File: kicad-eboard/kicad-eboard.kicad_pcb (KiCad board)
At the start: 2 copper layers, 89 parts, among them J1 Conn_02x03, J2 Conn_01x02, J3 Conn_01x10, M1 Hopper_Servo, SW1 LIMIT_1, SW2 LIMIT_2, SW3 SRX_Encoder, U1 TinkerBoard, U10 REF2033, U11 PDQ15-Q24-S12-D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

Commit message: Work from IPRO
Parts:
- C6, C7, R9, U6: moved to B.Cu
- moved TP2 66.1 mm to (133.5, 8.00)
- moved R4 65.5 mm to (140.0, 19.5)
- moved C5 58.1 mm to (132.8, 22.0), turned to 90 degrees
- moved R3 57.6 mm to (147.0, 19.5)
- moved U6 51.5 mm to (132.5, 22.0), turned to 90 degrees
- moved TP15 45.1 mm to (80.4, -9.20)
- moved TP9 45.1 mm to (80.4, -12.4)
- moved TP12 45.1 mm to (80.7, -2.40)
- moved TP11 45.1 mm to (78.0, 1.15)
- moved TP14 45.1 mm to (80.4, -5.95)
- moved TP13 43.6 mm to (80.0, -19.1)
- moved TP4 40.1 mm to (151.5, 26.8)
- moved R2 40.0 mm to (140.0, 28.0)
- moved TP10 38.0 mm to (114.0, 69.5)
- moved R9 33.7 mm to (137.2, 22.0), turned to 0 degrees
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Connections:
- C5 pad 1: +3V3 -> +3.3VADC
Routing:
- net /M3-: track 0.00 -> 24.1 mm
- net Net-(C7-Pad1): track 26.6 -> 2.70 mm, vias 0 -> 1
- net Net-(C7-Pad2): track 24.6 -> 2.53 mm, vias 0 -> 1
- net GNDREF: track 25.2 -> 4.04 mm
- net /M1-: track 0.00 -> 20.3 mm
- net Net-(C7-Pad3): track 22.4 -> 2.44 mm, vias 0 -> 1
- net /M3+: track 0.00 -> 17.6 mm
- net Net-(C7-Pad4): track 19.4 -> 2.54 mm, vias 0 -> 1
- net /M6+: track 16.4 -> 0.00 mm
- net /M5-: track 15.9 -> 0.00 mm
- net /M1+: track 0.00 -> 15.3 mm
- net /M5+: track 14.3 -> 0.00 mm
- net +1.65V: track 19.7 -> 6.09 mm, vias 3 -> 1
- net /M8-: track 16.6 -> 29.7 mm
- net /M2-: track 0.00 -> 11.3 mm
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- added copper zone on F.Cu, net +1.65V
- added copper zone on B.Cu, net GNDREF

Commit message: Add PTC fuse
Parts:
- added F1: 6A, 2019Spacehawks:Fuse_Littelfuse_16R600G, F.Cu at (82.0, 25.0)
- added H1: MountingHole, MountingHole:MountingHole_2.7mm_M2.5_Pad, F.Cu at (232.5, 69.0)
- added H2: MountingHole, MountingHole:MountingHole_2.7mm_M2.5_Pad, F.Cu at (232.5, 147.0)
- added H3: MountingHole, MountingHole:MountingHole_2.7mm_M2.5_Pad, F.Cu at (281.5, 69.0)
- added H4: MountingHole, MountingHole:MountingHole_2.7mm_M2.5_Pad, F.Cu at (281.5, 147.0)
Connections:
- J2 pad 1: +BATT -> Net-(F1-Pad1)
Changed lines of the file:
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@@
-(kicad_pcb (version 20171130) (host pcbnew "(5.1.5)-3")
+(kicad_pcb (version 20171130) (host pcbnew 5.0.2+dfsg1-1)
   (general
     (thickness 1.6)
@@
     (tracks 316)
     (zones 0)
-    (modules 89)
-    (nets 97)
+    (modules 94)
+    (nets 98)
   )
   (page A4)
@@
     (zone_45_only no)
     (trace_min 0.1778)
+    (segment_width 0.2)
+    (edge_width 0.15)
     (via_size 0.8)
     (via_drill 0.4)
@@
     (uvia_min_size 0.2)
     (uvia_min_drill 0.1)
-    (edge_width 0.15)
-    (segment_width 0.2)
     (pcb_text_width 0.3)
     (pcb_text_size 1.5 1.5)
@@
   (net 95 "Net-(C12-Pad1)")
   (net 96 "Net-(C11-Pad1)")
+  (net 97 "Net-(F1-Pad1)")
   (net_class Default "This is the default net class."
     (clearance 0.2)
@@
     (add_net "Net-(C7-Pad3)")
     (add_net "Net-(C7-Pad4)")
+    (add_net "Net-(F1-Pad1)")
     (add_net "Net-(M1-Pad1)")
     (add_net "Net-(M1-Pad4)")
@@
     (uvia_drill 0.1)
   )
+  (module 2019Spacehawks:Fuse_Littelfuse_16R600G (layer F.Cu)
+    (at 82 25)
+    (tags "PTC resettable fuse")
+    (fp_text reference F1 (at 0 0.5) (layer F.SilkS)
+      (effects (font (size 1 1) (thickness 0.15)))
+    )
+    (fp_text value 6A (at 0 -0.5) (layer F.Fab)
+      (effects (font (size 1 1) (thickness 0.15)))
+    )
+    (fp_line (start -5.2 -1.5) (end 5.2 -1.5) (layer F.SilkS) (width 0.15))
+    (fp_line (start 5.2 -1.5) (end 5.2 1.5) (layer F.SilkS) (width 0.15))
+    (fp_line (start -5.2 1.5) (end 5.2 1.5) (layer F.SilkS) (width 0.15))
+    (fp_line (start -5.2 -1.5) (end -5.2 1.5) (layer F.SilkS) (width 0.15))
+    (fp_line (start -5.4 -1.7) (end 5.4 -1.7) (layer F.CrtYd) (width 0.15))
+    (fp_line (start -5.4 -1.7) (end -5.4 1.7) (layer F.CrtYd) (width 0.15))
+    (fp_line (start -5.4 1.7) (end 5.4 1.7) (layer F.CrtYd) (width 0.15))
+    (fp_line (start 5.4 -1.7) (end 5.4 1.7) (layer F.CrtYd) (width 0.15))
+    (pad 1 thru_hole circle (at -2.55 -0.6) (size 1.524 1.524) (drill 0.83) (layers *.Cu *.Mask)
+      (net 97 "Net-(F1-Pad1)"))
+    (pad 2 thru_hole circle (at 2.55 0.6) (size 1.524 1.524) (drill 0.83) (layers *.Cu *.Mask)
+      (net 3 +BATT))
+  )
+  (module MountingHole:MountingHole_2.7mm_M2.5_Pad (layer F.Cu)
+    (at 281.5 147)
+    (descr "Mounting Hole 2.7mm, M2.5")
+    (tags "mounting hole 2.7mm m2.5")
+    (attr virtual)
+    (fp_text reference H4 (at 0 -3.7) (layer F.SilkS)
+      (effects (font (size 1 1) (thickness 0.15)))
+    )
+    (fp_text value MountingHole (at 0 3.7) (layer F.Fab)
+      (effects (font (size 1 1) (thickness 0.15)))
+    )
+    (fp_circle (center 0 0) (end 2.95 0) (layer F.CrtYd) (width 0.05))
+    (fp_circle (center 0 0) (end 2.7 0) (layer Cmts.User) (width 0.15))
+    (fp_text user %R (at 0.3 0) (layer F.Fab)
+      (effects (font (size 1 1) (thickness 0.15)))
+    )
+    (pad 1 thru_hole circle (at 0 0) (size 5.4 5.4) (drill 2.7) (layers *.Cu *.Mask))
+  )
+  (module MountingHole:MountingHole_2.7mm_M2.5_Pad (layer F.Cu)
+    (at 281.5 69)
+    (descr "Mounting Hole 2.7mm, M2.5")
+    (tags "mounting hole 2.7mm m2.5")
+    (attr virtual)
+    (fp_text reference H3 (at 0 -3.7) (layer F.SilkS)
+      (effects (font (size 1 1) (thickness 0.15)))
+    )
+    (fp_text value MountingHole (at 0 3.7) (layer F.Fab)
+      (effects (font (size 1 1) (thickness 0.15)))
+    )
+    (fp_text user %R (at 0.3 0) (layer F.Fab)
+      (effects (font (size 1 1) (thickness 0.15)))
+    )
+    (fp_circle (center 0 0) (end 2.7 0) (layer Cmts.User) (width 0.15))
+    (fp_circle (center 0 0) (end 2.95 0) (layer F.CrtYd) (width 0.05))
+    (pad 1 thru_hole circle (at 0 0) (size 5.4 5.4) (drill 2.7) (layers *.Cu *.Mask))
+  )
+  (module MountingHole:MountingHole_2.7mm_M2.5_Pad (layer F.Cu)
+    (at 232.5 147)
+    (descr "Mounting Hole 2.7mm, M2.5")
+    (tags "mounting hole 2.7mm m2.5")
+    (attr virtual)
+    (fp_text reference H2 (at 0 -3.7) (layer F.SilkS)
+      (effects (font (size 1 1) (thickness 0.15)))
+    )
+    (fp_text value MountingHole (at 0 3.7) (layer F.Fab)
+      (effects (font (size 1 1) (thickness 0.15)))
+    )
+    (fp_circle (center 0 0) (end 2.95 0) (layer F.CrtYd) (width 0.05))
+    (fp_circle (center 0 0) (end 2.7 0) (layer Cmts.User) (width 0.15))
+    (fp_text user %R (at 0.3 0) (layer F.Fab)
+      (effects (font (size 1 1) (thickness 0.15)))
+    )
+    (pad 1 thru_hole circle (at 0 0) (size 5.4 5.4) (drill 2.7) (layers *.Cu *.Mask))
+  )
+  (module MountingHole:MountingHole_2.7mm_M2.5_Pad (layer F.Cu)
+    (at 232.5 69)
+    (descr "Mounting Hole 2.7mm, M2.5")
+    (tags "mounting hole 2.7mm m2.5")
+    (attr virtual)
+    (fp_text reference H1 (at 0 -3.7) (layer F.SilkS)
+      (effects (font (size 1 1) (thickness 0.15)))
+    )
+    (fp_text value MountingHole (at 0 3.7) (layer F.Fab)
+      (effects (font (size 1 1) (thickness 0.15)))
+    )
+    (fp_text user %R (at 0.3 0) (layer F.Fab)
+      (effects (font (size 1 1) (thickness 0.15)))
+    )
+    (fp_circle (center 0 0) (end 2.7 0) (layer Cmts.User) (width 0.15))
+    (fp_circle (center 0 0) (end 2.95 0) (layer F.CrtYd) (width 0.05))
+    (pad 1 thru_hole circle (at 0 0) (size 5.4 5.4) (drill 2.7) (layers *.Cu *.Mask))
+  )
   (module Package_SO:TSSOP-20_4.4x6.5mm_P0.65mm (layer F.Cu)
     (at 132.5 30 90)
@@
       (net 2 GNDPWR))
     (pad 1 thru_hole rect (at -3.95 0 270) (size 6.25 2.25) (drill oval 5.23 1.27) (layers *.Cu *.Mask)
-      (net 3 +BATT))
+      (net 97 "Net-(F1-Pad1)"))
     (model ${KIPRJMOD}/2019Spacehawks.pretty/Powerpole_45A_Vert_01x02.wrl
       (at (xyz 0 0 0))
@@
   (gr_arc (start 281.5 69) (end 285 69) (angle -90) (layer F.SilkS) (width 0.2))
   (gr_arc (start 232.5 69) (end 232.5 65.5) (angle -90) (layer F.SilkS) (width 0.2))
-  (gr_line (start 285 150.5) (end 232.5 150.5) (layer F.SilkS) (width 0.2))
-  (gr_line (start 285 69) (end 285 150.5) (layer F.SilkS) (width 0.2))
+  (gr_line (start 281.5 150.5) (end 232.5 150.5) (layer F.SilkS) (width 0.2))
+  (gr_line (start 285 69) (end 285 147) (layer F.SilkS) (width 0.2))
   (gr_line (start 232.5 65.5) (end 281.5 65.5) (layer F.SilkS) (width 0.2))
   (gr_line (start 229 147) (end 229 69) (layer F.SilkS) (width 0.2))

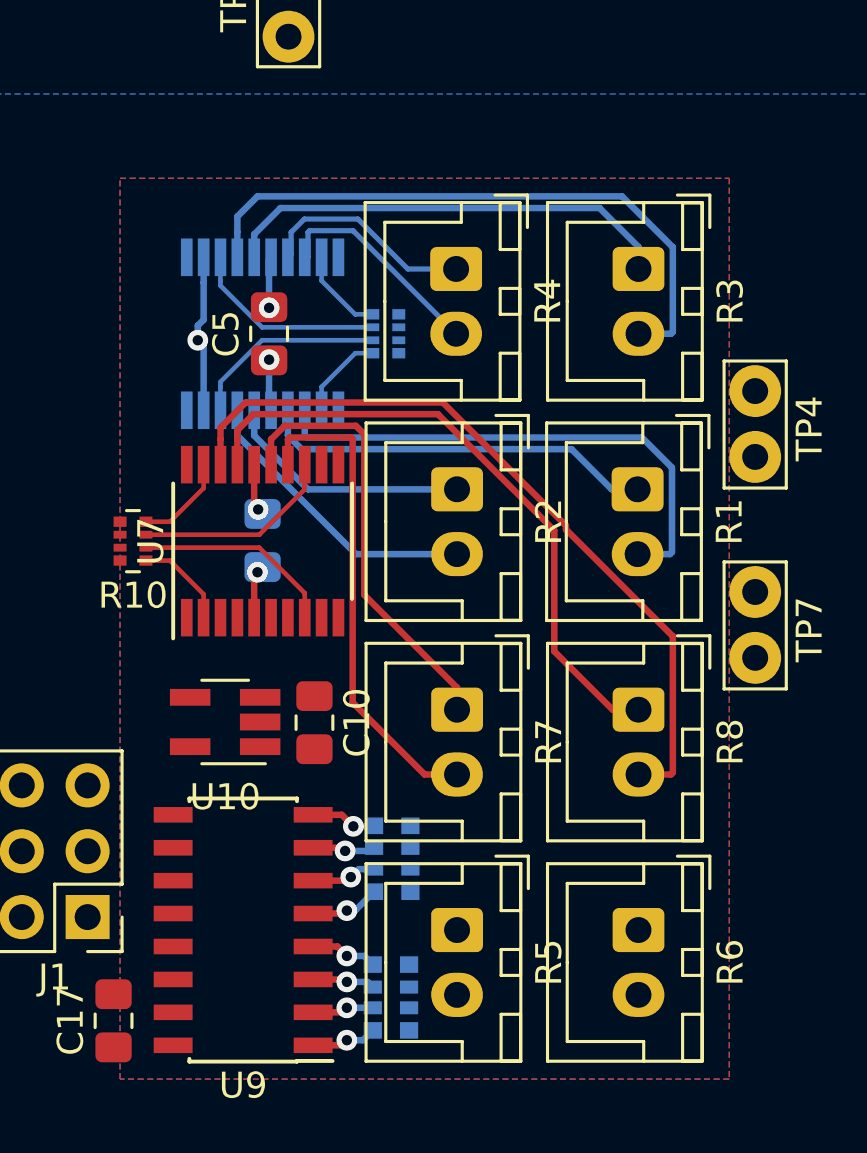
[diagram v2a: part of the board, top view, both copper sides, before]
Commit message: Route differential pairs
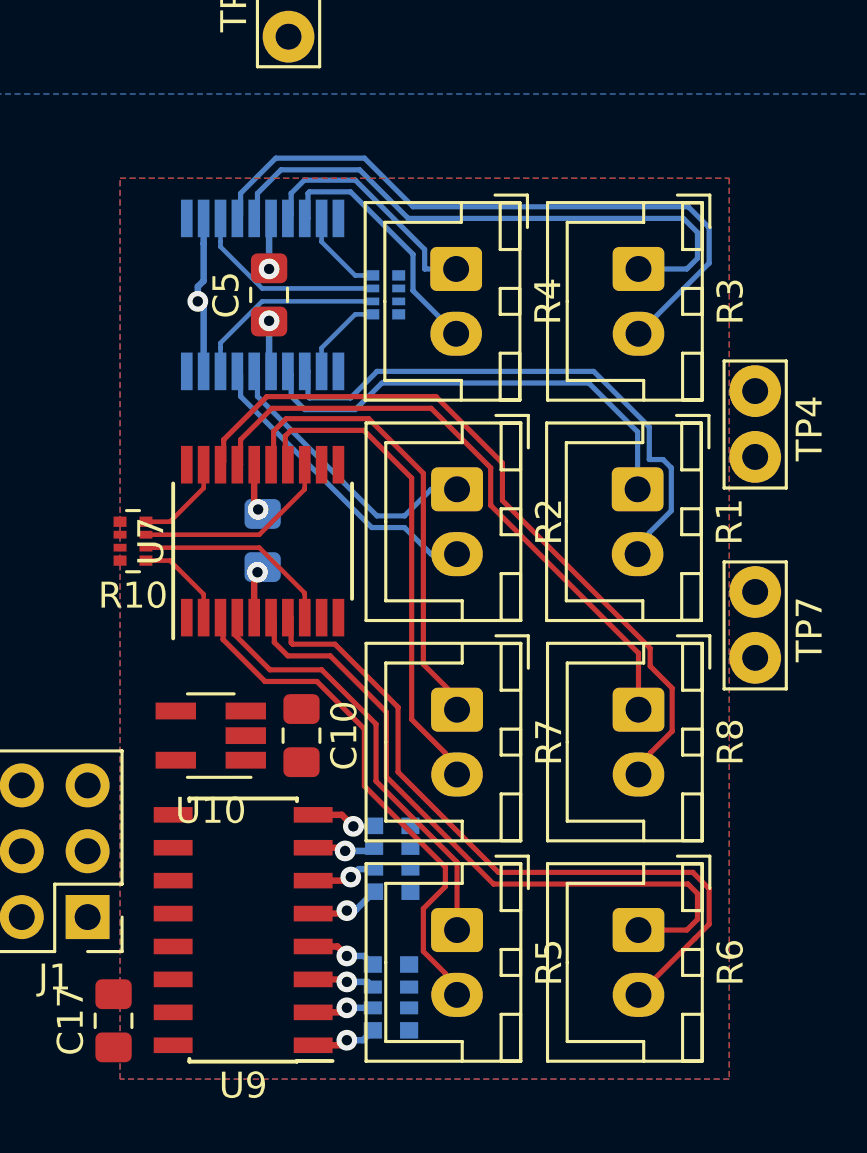
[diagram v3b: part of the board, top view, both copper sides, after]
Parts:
- moved C5 1.50 mm to (132.8, 20.5)
- moved R9 1.50 mm to (137.2, 20.5)
- moved U6 1.50 mm to (132.5, 20.5)
- moved U10 0.76 mm to (130.5, 37.5)
- moved C10 0.71 mm to (134.0, 37.5)
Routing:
- net /M6-: track 0.00 -> 27.8 mm
- net /M6+: track 0.00 -> 26.2 mm
- net /M5-: track 0.00 -> 20.2 mm
- net /M5+: track 0.00 -> 16.8 mm
- net /M3+: track 17.6 -> 22.9 mm
- net /M1+: track 15.3 -> 18.0 mm
- net /M3-: track 24.1 -> 26.0 mm
- net /M4-: track 8.48 -> 9.92 mm
- net /M1-: track 20.3 -> 21.7 mm
- net /M2+: track 9.66 -> 11.1 mm
- net /M4+: track 8.39 -> 9.45 mm
- net /M8-: track 29.7 -> 28.8 mm
- net /M7+: track 17.0 -> 17.8 mm
- net /M8+: track 24.5 -> 23.9 mm
- net /M2-: track 11.3 -> 11.9 mm

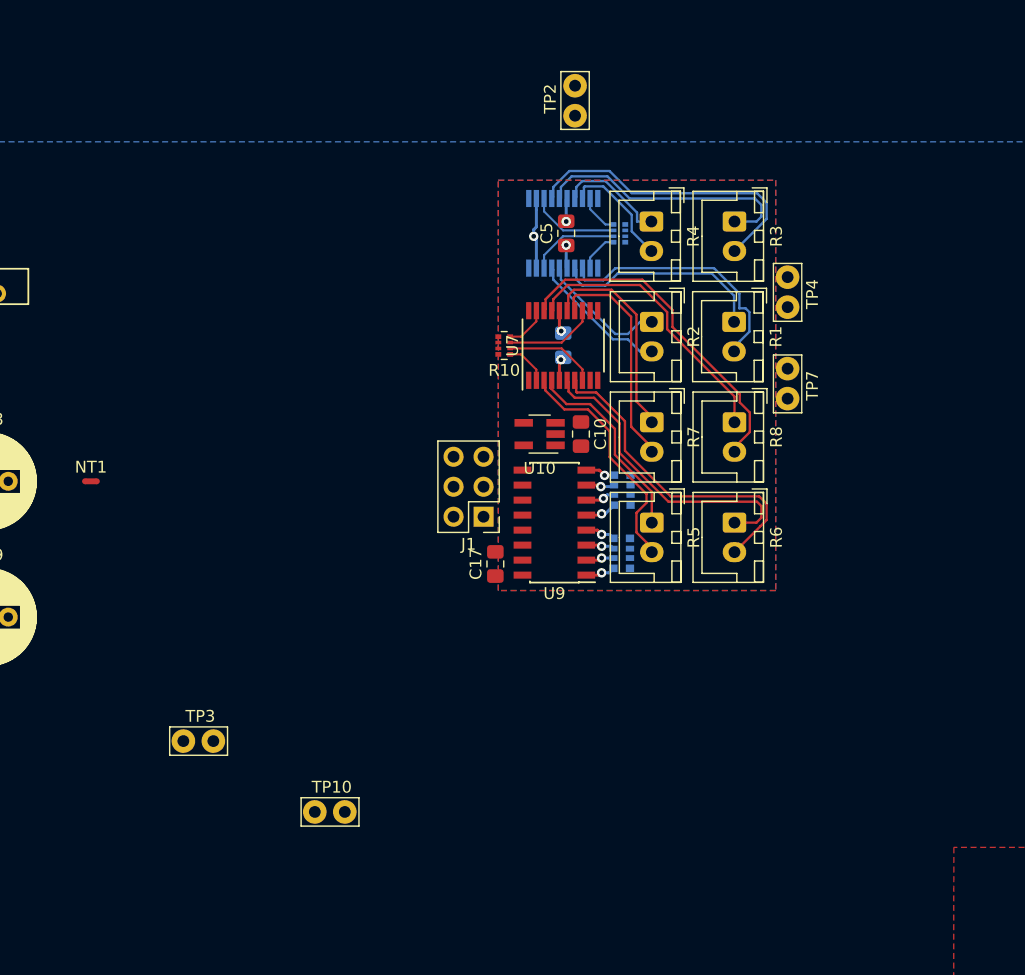
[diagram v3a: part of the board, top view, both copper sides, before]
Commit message: Current sense routing take 2
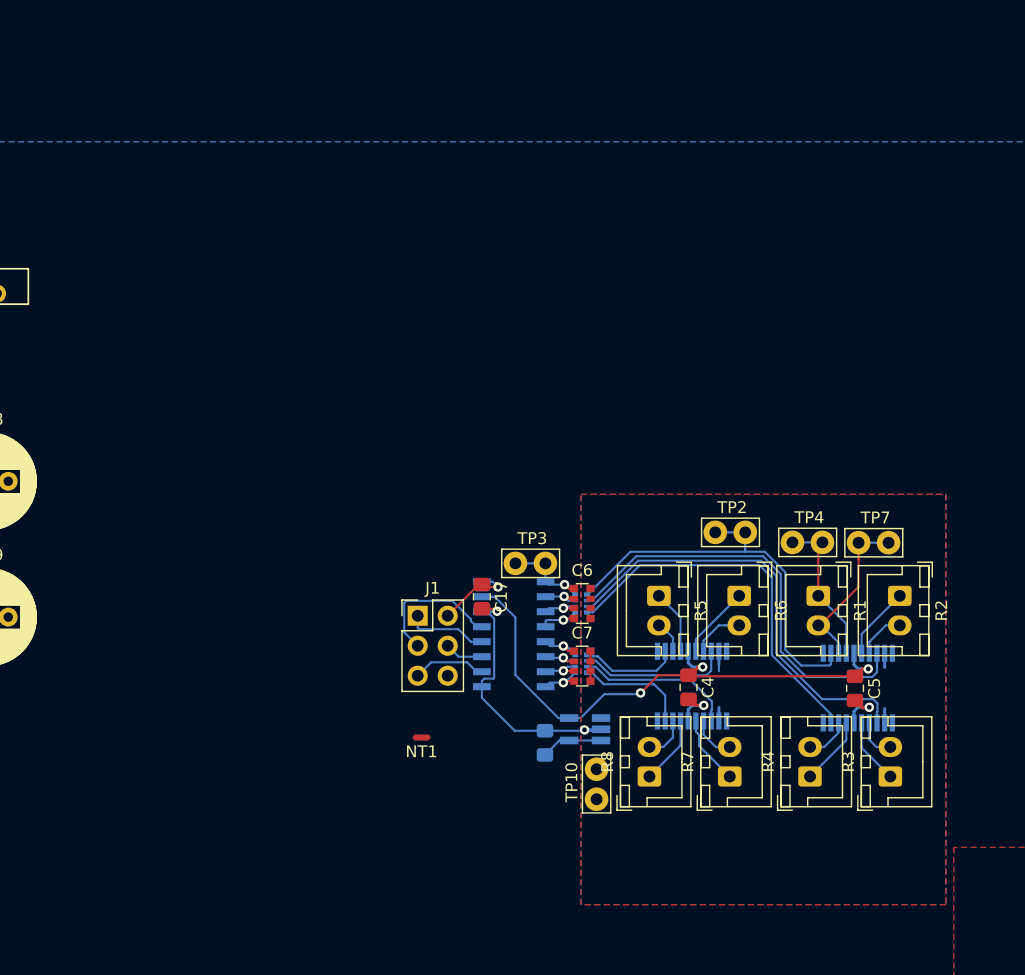
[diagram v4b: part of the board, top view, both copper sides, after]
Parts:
- C10, R10, U10, U7, U9: moved to B.Cu
- C4, C6, C7: moved to F.Cu
- moved R4 48.9 mm to (153.4, 66.5), turned to 90 degrees
- moved R3 48.8 mm to (160.2, 66.5), turned to 90 degrees
- moved U6 45.9 mm to (157.4, 59.0), turned to 270 degrees
- moved C5 45.6 mm to (157.2, 59.0), turned to 270 degrees
- moved TP2 40.5 mm to (147.9, 45.8), turned to 180 degrees
- moved NT1 35.4 mm to (120.5, 63.2), turned to 180 degrees
- moved TP3 31.9 mm to (131.0, 48.5)
- moved R9 31.5 mm to (134.0, 51.8), turned to 180 degrees
- moved R2 31.3 mm to (161.0, 51.2)
- moved C4 30.9 mm to (143.1, 58.9), turned to 270 degrees
- moved R8 30.9 mm to (139.8, 66.5), turned to 90 degrees
- moved U7 30.8 mm to (143.4, 58.8), turned to 270 degrees
- moved R7 30.7 mm to (146.6, 66.5), turned to 90 degrees
- moved R10 27.7 mm to (134.0, 56.9)
- moved C10 26.3 mm to (130.9, 63.6), turned to 90 degrees
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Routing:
- net +3.3VADC: track 4.09 -> 47.8 mm, vias 2 -> 3
- net Net-(R9-Pad1): track 3.42 -> 35.1 mm
- net GNDREF: track 4.04 -> 34.7 mm, vias 2 -> 4
- net Net-(R9-Pad3): track 7.63 -> 36.7 mm
- net Net-(R9-Pad4): track 3.42 -> 32.1 mm
- net Net-(R9-Pad2): track 7.63 -> 36.0 mm
- net /M8-: track 28.8 -> 3.71 mm
- net /M6-: track 27.8 -> 4.46 mm
- net /M3-: track 26.0 -> 3.46 mm
- net /M6+: track 26.2 -> 6.22 mm
- net /M8+: track 23.9 -> 5.79 mm
- net /M5-: track 20.2 -> 2.78 mm
- net /M3+: track 22.9 -> 5.54 mm
- net /M7-: track 19.0 -> 3.81 mm
- net /M7+: track 17.8 -> 5.89 mm
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- added copper zone on B.Cu, net +1.65V
- added copper zone on F.Cu, net GNDREF
- removed copper zone on F.Cu, net +1.65V
- removed copper zone on B.Cu, net GNDREF

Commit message: More routing
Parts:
- NT1: moved to B.Cu
- moved H1 141.6 mm to (99.8, 19.7)
- moved H2 141.6 mm to (99.8, 97.7)
- moved H3 141.6 mm to (148.8, 19.7)
- moved H4 141.6 mm to (148.8, 97.7)
- moved R3 92.3 mm to (71.7, 92.6), turned to 0 degrees
- moved R2 85.2 mm to (87.0, 93.4), turned to 180 degrees
- moved U6 84.2 mm to (79.1, 89.8), turned to 180 degrees
- moved R4 84.0 mm to (71.7, 85.8), turned to 0 degrees
- moved C5 83.9 mm to (79.1, 89.6), turned to 180 degrees
- moved TP7 82.5 mm to (91.5, 92.5), turned to 90 degrees
- moved R7 76.0 mm to (71.7, 79.0), turned to 0 degrees
- moved R1 75.9 mm to (87.0, 86.5), turned to 180 degrees
- moved M1 75.2 mm to (75.3, 102.1), turned to 180 degrees
- moved TP4 74.7 mm to (91.5, 86.8), turned to 90 degrees
- moved C3 71.6 mm to (82.8, 102.5), turned to 90 degrees
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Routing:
- net /SDA: track 38.8 -> 28.3 mm
- net /SCL: track 48.0 -> 38.8 mm
- removed copper zone on B.Cu, net GND
